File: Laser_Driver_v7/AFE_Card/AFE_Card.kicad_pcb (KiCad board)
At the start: 2 copper layers, 160 x 100 mm, 137 parts, among them J1 DIN41612_03x32_C_Split, J204 LO1 ref SMA, J205 LO2 ref SMA, U1 LT3042EMSE +12V, U201 ADS1115, U202 OPA192IDBVR ERR1 buffer, U203 OPA192IDBVR ERR2 buffer, U204 OPA820 LOx3, U205 OPA820 LOx3, U206 AD5696R, U30 OPA814DBVR, U31 OPA814DBVR, U45 AD835 demod, U46 AD835 demod

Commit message: Working towards a full set of pcbs in v7
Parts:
- U1: footprint Package_SO:MSOP-10-1EP_3x3mm_P0.5mm_EP2.2x3.1mm_Mask1.83x1.89mm_ThermalVias -> Package_SO:MSOP-10-1EP_3x3mm_P0.5mm_EP1.68x1.88mm
- moved TP412 28.4 mm to (158.1, 52.0)
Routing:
- net 5Vref: track 239.4 -> 283.8 mm, vias 6 -> 7
- net SCL_BUS: track 10.2 -> 35.4 mm, vias 0 -> 2
- net GND: track 54.5 -> 29.3 mm
- net ERR2_BUS: track 7.01 -> 32.0 mm, vias 0 -> 2
- net SDA_BUS: track 10.1 -> 32.9 mm, vias 0 -> 2
- net VREF_MID: track 91.8 -> 113.5 mm, vias 3 -> 5
- net ERR1_BUS: track 86.2 -> 106.5 mm, vias 2 -> 4
- net FAULT_n: track 200.8 -> 208.9 mm, vias 3 -> 5
- net -15V: track 96.5 -> 102.4 mm, vias 4 -> 6
- net 1V8: track 0.00 -> 5.16 mm
- net +5V_LASER: track 0.00 -> 5.12 mm
- net -18V: track 0.00 -> 5.08 mm
- net +18V: track 0.00 -> 5.08 mm
- net +15V: track 214.6 -> 219.3 mm, vias 4 -> 6
- net 3V3: track 60.3 -> 63.2 mm
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
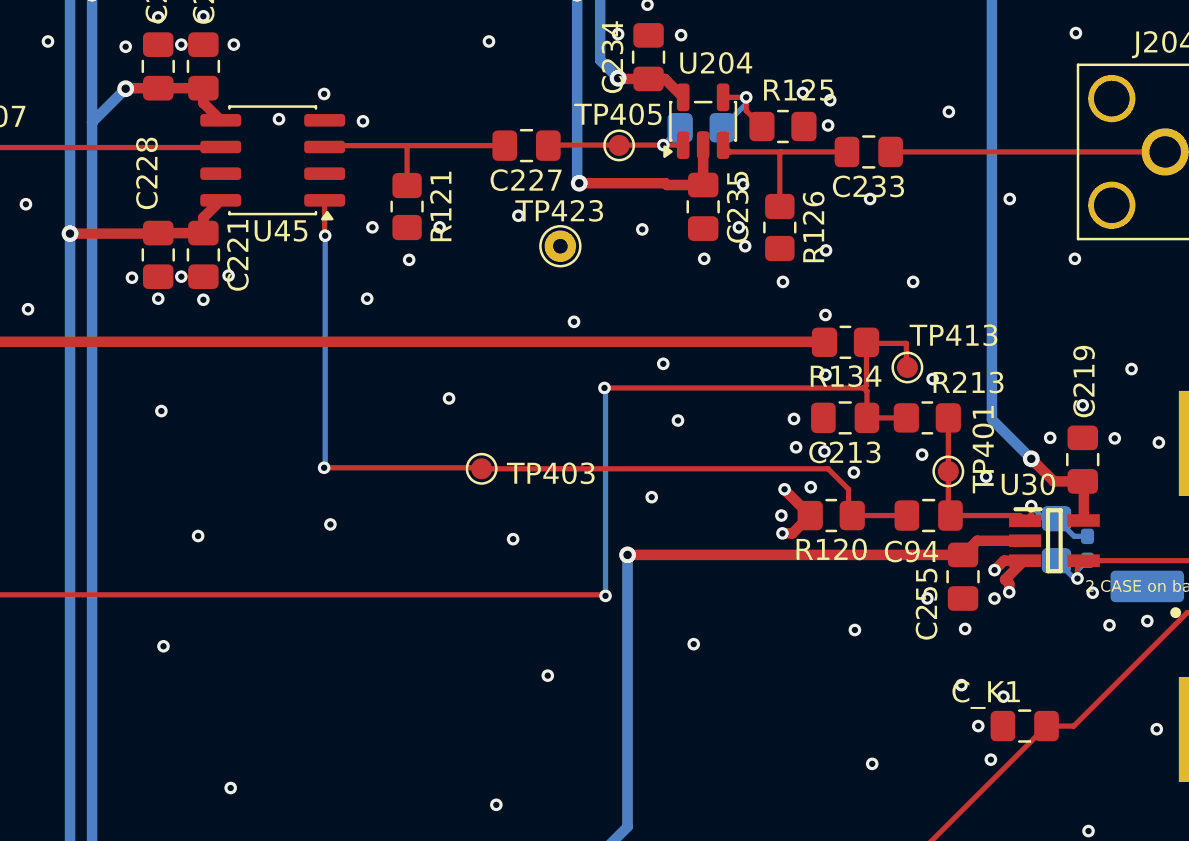
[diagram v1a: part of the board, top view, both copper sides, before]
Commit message: Updates to capacitors for derating.
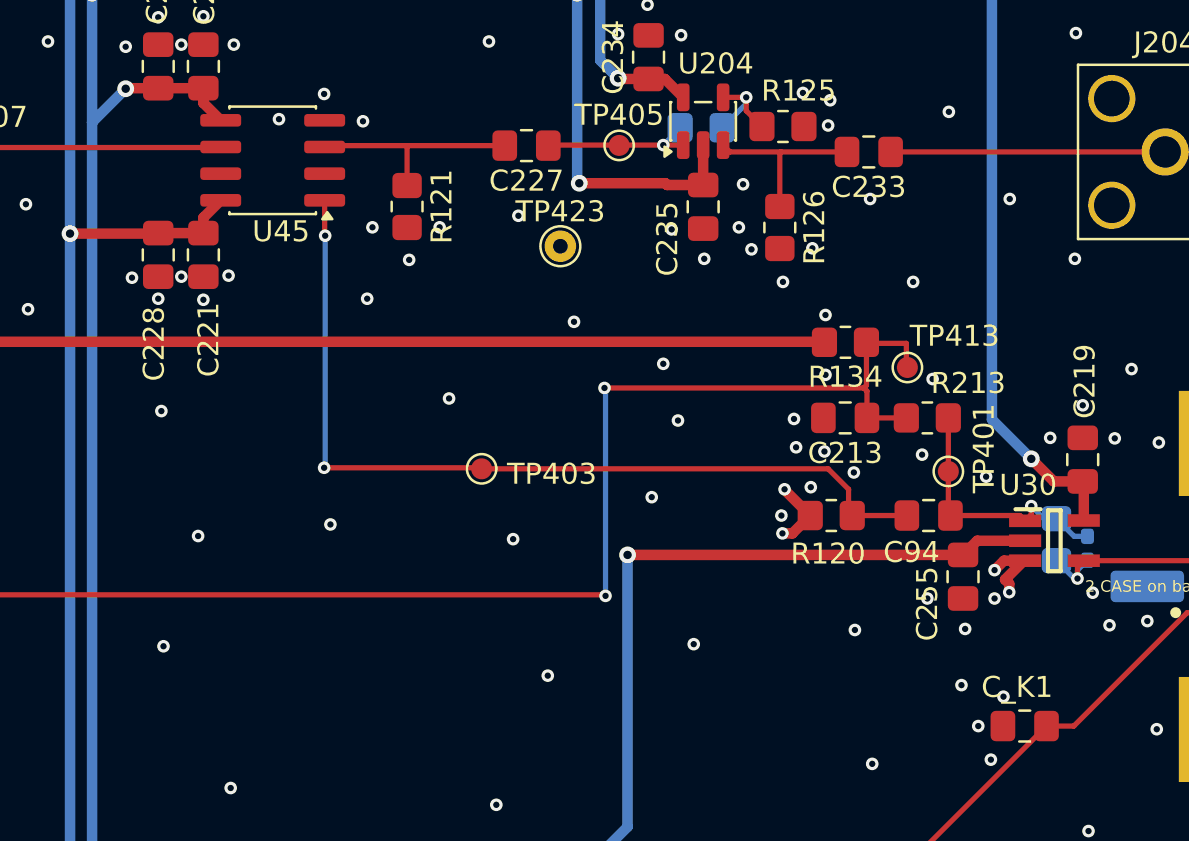
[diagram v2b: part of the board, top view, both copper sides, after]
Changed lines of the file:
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@@
 		)
 		(property "Value" "LO1_BUF"
-			(at 0 1.55 0)
+			(at -1.2 -1.5 0)
 			(layer "F.Fab")
 			(effects
@@
 		(tags "capacitor handsolder")
 		(property "Reference" "C_K1"
-			(at 1.8125 1.6 0)
+			(at 0.3625 1.85 0)
 			(layer "F.SilkS")
 			(effects
@@
 		(attr smd)
 		(duplicate_pad_numbers_are_jumpers no)
-			(fp_line
+		(fp_line
 			(start -1.61 -1.61)
 			(end 1.61 -1.61)
@@
 			(layer "F.SilkS")
 		)
-			(fp_line
+		(fp_line
 			(start -1.61 -1.41)
 			(end -1.61 -1.61)
@@
 			(layer "F.SilkS")
 		)
-			(fp_line
+		(fp_line
 			(start -1.61 1.61)
 			(end -1.61 1.41)
@@
 			(layer "F.SilkS")
 		)
-			(fp_line
+		(fp_line
 			(start 1.61 -1.61)
 			(end 1.61 -1.41)
@@
 			(layer "F.SilkS")
 		)
-			(fp_line
+		(fp_line
 			(start 1.61 1.41)
 			(end 1.61 1.61)
@@
 			(layer "F.SilkS")
 		)
-			(fp_line
+		(fp_line
 			(start 1.61 1.61)
 			(end -1.61 1.61)
@@
 			(layer "F.SilkS")
 		)
-			(fp_poly
+		(fp_poly
 			(pts
-				(xy -2.16 -1.41)
-				(xy -2.4 -1.74)
-				(xy -1.92 -1.74)
+				(xy -2.16 -1.41) (xy -2.4 -1.74) (xy -1.92 -1.74)
 			)
 			(stroke
@@
 			(layer "F.SilkS")
 		)
-			(fp_line
+		(fp_line
 			(start -3.13 -1.4)
 			(end -1.75 -1.4)
@@
 			(layer "F.CrtYd")
 		)
-			(fp_line
+		(fp_line
 			(start -3.13 1.4)
 			(end -3.13 -1.4)
@@
 			(layer "F.CrtYd")
 		)
-			(fp_line
+		(fp_line
 			(start -1.75 -1.75)
 			(end 1.75 -1.75)
@@
 			(layer "F.CrtYd")
 		)
-			(fp_line
+		(fp_line
 			(start -1.75 -1.4)
 			(end -1.75 -1.75)
@@
 			(layer "F.CrtYd")
 		)
-			(fp_line
+		(fp_line
 			(start -1.75 1.4)
 			(end -3.13 1.4)
@@
 			(layer "F.CrtYd")
 		)
-			(fp_line
+		(fp_line
 			(start -1.75 1.75)
 			(end -1.75 1.4)
@@
 			(layer "F.CrtYd")
 		)
-			(fp_line
+		(fp_line
 			(start 1.75 -1.75)
 			(end 1.75 -1.4)
@@
 			(layer "F.CrtYd")
 		)
-			(fp_line
+		(fp_line
 			(start 1.75 -1.4)
 			(end 3.13 -1.4)
@@
 			(layer "F.CrtYd")
 		)
-			(fp_line
+		(fp_line
 			(start 1.75 1.4)
 			(end 1.75 1.75)
@@
 			(layer "F.CrtYd")
 		)
-			(fp_line
+		(fp_line
 			(start 1.75 1.75)
 			(end -1.75 1.75)
@@
 			(layer "F.CrtYd")
 		)
-			(fp_line
+		(fp_line
 			(start 3.13 -1.4)
 			(end 3.13 1.4)
@@
 			(layer "F.CrtYd")
 		)
-			(fp_line
+		(fp_line
 			(start 3.13 1.4)
 			(end 1.75 1.4)
@@
 			(layer "F.CrtYd")
 		)
-			(fp_poly
+		(fp_poly
 			(pts
-				(xy -0.75 -1.5)
-				(xy 1.5 -1.5)
-				(xy 1.5 1.5)
-				(xy -1.5 1.5)
-				(xy -1.5 -0.75)
+				(xy -0.75 -1.5) (xy 1.5 -1.5) (xy 1.5 1.5) (xy -1.5 1.5) (xy -1.5 -0.75)
 			)
 			(stroke
@@
 			)
 		)
+		(pad "" smd roundrect
+			(at -0.42 -0.47)
+			(size 0.68 0.76)
+			(layers "F.Paste")
+			(roundrect_rratio 0.25)
+		)
+		(pad "" smd roundrect
+			(at -0.42 0.47)
+			(size 0.68 0.76)
+			(layers "F.Paste")
+			(roundrect_rratio 0.25)
+		)
+		(pad "" smd roundrect
+			(at 0.42 -0.47)
+			(size 0.68 0.76)
+			(layers "F.Paste")
+			(roundrect_rratio 0.25)
+		)
+		(pad "" smd roundrect
+			(at 0.42 0.47)
+			(size 0.68 0.76)
+			(layers "F.Paste")
+			(roundrect_rratio 0.25)
+		)
 		(pad "1" smd roundrect
 			(at -2.15 -1)
@@
 			(pintype "power_out")
 		)
-		(embedded_fonts no)
-			(pad "" smd roundrect
-			(at -0.42 -0.47)
-			(size 0.68 0.76)
-			(layers "F.Paste")
-			(roundrect_rratio 0.25)
-		)
-			(pad "" smd roundrect
-			(at -0.42 0.47)
-			(size 0.68 0.76)
-			(layers "F.Paste")
-			(roundrect_rratio 0.25)
-		)
-			(pad "" smd roundrect
-			(at 0.42 -0.47)
-			(size 0.68 0.76)
-			(layers "F.Paste")
-			(roundrect_rratio 0.25)
-		)
-			(pad "" smd roundrect
-			(at 0.42 0.47)
-			(size 0.68 0.76)
-			(layers "F.Paste")
-			(roundrect_rratio 0.25)
-		)
-			(pad "11" smd rect
+		(pad "11" smd rect
 			(at 0 0)
 			(size 1.68 1.88)
@@
 			(zone_connect 2)
 		)
+		(embedded_fonts no)
 		(model "${KICAD10_3DMODEL_DIR}/Package_SO.3dshapes/MSOP-10-1EP_3x3mm_P0.5mm_EP2.2x3.1mm_Mask1.83x1.89mm.step"
 			(offset
@@
 		(tags "capacitor handsolder")
 		(property "Reference" "C235"
-			(at 0 -1.68 90)
+			(at 1.5275 1.7 90)
 			(layer "F.SilkS")
 			(effects
@@
 		(tags "capacitor handsolder")
 		(property "Reference" "C228"
-			(at -3.8875 0.5 90)
+			(at 4.2375 0.2 90)
 			(layer "F.SilkS")
 			(effects
@@
 		(tags "capacitor handsolder")
 		(property "Reference" "C221"
-			(at 0 -1.68 90)
+			(at 4.0375 -0.25 90)
 			(layer "F.SilkS")
 			(effects
@@
 		(tags "resistor handsolder")
 		(property "Reference" "R120"
-			(at 0 -1.65 0)
+			(at 0.15 -1.825 0)
 			(layer "F.SilkS")
 			(effects
@@
 	)
 	(via
-		(at 210.35 47.6)
+		(at 209.7 47.5)
 		(size 0.6)
 		(drill 0.3)
@@
 	)
 	(via
-		(at 206.5 47.4)
+		(at 206.8 47.55)
 		(size 0.6)
 		(drill 0.3)
@@
 	)
 	(via
-		(at 201.6 46.6)
+		(at 203 46.6)
 		(size 0.6)
 		(drill 0.3)

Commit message: minor updates and U for FBG
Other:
- board text added: "AFE_Card v7"
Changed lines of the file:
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@@
 	)
 	(embedded_fonts no)
+	(gr_text "AFE_Card v7"
+		(at 123.225 30.500 0)
+		(layer "B.SilkS")
+		(effects
+			(font
+				(size 1.5 1.5)
+				(thickness 0.25)
+			)
+			(justify mirror)
+		)
+	)
 )
